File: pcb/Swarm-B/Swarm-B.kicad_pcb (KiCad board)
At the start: 2 copper layers, 71.9 x 71.9 mm, 26 parts, among them J1 RX_Break, J2 5v_3Pi, J3 GND_3Pi, J4 I2C_3Pi, SW1 Bttn, U1 74LS32, U2 TSDP34138

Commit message: added sda and scl labels to pcb
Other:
- board text added: "SCL"
- board text added: "SDA"
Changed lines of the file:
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@@
   (general
     (thickness 1.6)
-    (drawings 15)
+    (drawings 17)
     (tracks 217)
     (zones 0)
@@
   (page A4)
   (layers
-    (0 F.Cu signal)
-    (31 B.Cu signal)
+    (0 F.Cu signal hide)
+    (31 B.Cu signal hide)
     (32 B.Adhes user hide)
     (33 F.Adhes user hide)
@@
     (visible_elements 7FFFFFFF)
     (pcbplotparams
-      (layerselection 0x010fc_ffffffff)
+      (layerselection 0x01030_ffffffff)
       (usegerberextensions false)
       (usegerberattributes false)
@@
       (outputformat 1)
       (mirror false)
-      (drillshape 1)
+      (drillshape 0)
       (scaleselection 1)
-      (outputdirectory ""))
+      (outputdirectory "Gerbers/"))
   )
   (net 0 "")
@@
     )
   )
+  (gr_text SDA (at 127 105.664 90) (layer B.SilkS)
+    (effects (font (size 1.5 1.5) (thickness 0.3)) (justify mirror))
+  )
+  (gr_text SCL (at 129.794 105.664 90) (layer B.SilkS)
+    (effects (font (size 1.5 1.5) (thickness 0.3)) (justify mirror))
+  )
   (gr_text BLK (at 123.19 86.614) (layer B.SilkS)
     (effects (font (size 1.5 1.5) (thickness 0.3)) (justify mirror))
@@
   (segment (start 133.48863 75.438) (end 132.08 75.438) (width 0.25) (layer F.Cu) (net 0))
   (segment (start 134.62 75.438) (end 133.48863 75.438) (width 0.25) (layer F.Cu) (net 0))
-  (via (at 135.636 126.492) (size 0.8) (drill 0.4) (layers F.Cu B.Cu) (net 33))
-  (via (at 129.286 94.234) (size 0.8) (drill 0.4) (layers F.Cu B.Cu) (net 33))
-  (via (at 114.554 99.568) (size 0.8) (drill 0.4) (layers F.Cu B.Cu) (net 33))
-  (via (at 119.634 71.374) (size 0.8) (drill 0.4) (layers F.Cu B.Cu) (net 33))
   (segment (start 123.760001 120.333999) (end 124.46 119.634) (width 0.25) (layer F.Cu) (net 4))
   (segment (start 123.434999 120.659001) (end 123.760001 120.333999) (width 0.25) (layer F.Cu) (net 4))
@@
   (segment (start 124.46 113.564051) (end 120.447011 109.551062) (width 0.25) (layer B.Cu) (net 32))
   (segment (start 124.46 114.554) (end 124.46 113.564051) (width 0.25) (layer B.Cu) (net 32))
+  (via (at 135.636 126.492) (size 0.8) (drill 0.4) (layers F.Cu B.Cu) (net 33))
+  (via (at 129.286 94.234) (size 0.8) (drill 0.4) (layers F.Cu B.Cu) (net 33))
+  (via (at 114.554 99.568) (size 0.8) (drill 0.4) (layers F.Cu B.Cu) (net 33))
+  (via (at 119.634 71.374) (size 0.8) (drill 0.4) (layers F.Cu B.Cu) (net 33))
   (segment (start 129.54 86.614) (end 127 86.614) (width 0.25) (layer F.Cu) (net 33))
   (segment (start 145.571001 86.389001) (end 144.526 85.344) (width 0.25) (layer F.Cu) (net 33))

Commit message: update to readme
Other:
- board text added: "github.com/paulodowd/Swarm-Bs"
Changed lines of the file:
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@@
   (general
     (thickness 1.6)
-    (drawings 17)
+    (drawings 18)
     (tracks 217)
     (zones 0)
@@
     (36 B.SilkS user)
     (37 F.SilkS user)
-    (38 B.Mask user hide)
-    (39 F.Mask user hide)
+    (38 B.Mask user)
+    (39 F.Mask user)
     (40 Dwgs.User user hide)
     (41 Cmts.User user hide)
@@
     (visible_elements 7FFFFFFF)
     (pcbplotparams
-      (layerselection 0x01030_ffffffff)
+      (layerselection 0x010f0_ffffffff)
       (usegerberextensions false)
       (usegerberattributes false)
@@
     (descr "LED, diameter 3.0mm z-position of LED center 2.0mm, 2 pins")
     (tags "LED diameter 3.0mm z-position of LED center 2.0mm 2 pins")
-    (fp_text reference D1 (at 1.27 -1.96 18) (layer F.SilkS)
-      (effects (font (size 1 1) (thickness 0.15)))
-    )
-    (fp_text value IR_LED (at 0.941884 -2.89882 18) (layer F.Fab)
+    (fp_text reference D1 (at -1.521803 0.573822 18) (layer F.SilkS)
+      (effects (font (size 1 1) (thickness 0.15)))
+    )
+    (fp_text value IR_LED (at 5.706955 0.518945 18) (layer F.Fab)
       (effects (font (size 1 1) (thickness 0.15)))
     )
@@
     (descr "Resistor, Axial_DIN0204 series, Axial, Horizontal, pin pitch=5.08mm, 0.167W, length*diameter=3.6*1.6mm^2, http://cdn-reichelt.de/documents/datenblatt/B400/1_4W%23YAG.pdf")
     (tags "Resistor Axial_DIN0204 series Axial Horizontal pin pitch 5.08mm 0.167W length 3.6mm diameter 1.6mm")
-    (fp_text reference R2 (at 2.54 -1.92 90) (layer F.SilkS)
+    (fp_text reference R2 (at -1.524 0 90) (layer F.SilkS)
       (effects (font (size 1 1) (thickness 0.15)))
     )
@@
     (descr "Resistor, Axial_DIN0204 series, Axial, Horizontal, pin pitch=5.08mm, 0.167W, length*diameter=3.6*1.6mm^2, http://cdn-reichelt.de/documents/datenblatt/B400/1_4W%23YAG.pdf")
     (tags "Resistor Axial_DIN0204 series Axial Horizontal pin pitch 5.08mm 0.167W length 3.6mm diameter 1.6mm")
-    (fp_text reference R3 (at 2.54 -1.92 90) (layer F.SilkS)
+    (fp_text reference R3 (at -1.524 0 90) (layer F.SilkS)
       (effects (font (size 1 1) (thickness 0.15)))
     )
@@
     (descr "Resistor, Axial_DIN0204 series, Axial, Horizontal, pin pitch=5.08mm, 0.167W, length*diameter=3.6*1.6mm^2, http://cdn-reichelt.de/documents/datenblatt/B400/1_4W%23YAG.pdf")
     (tags "Resistor Axial_DIN0204 series Axial Horizontal pin pitch 5.08mm 0.167W length 3.6mm diameter 1.6mm")
-    (fp_text reference R4 (at 2.54 -1.92 90) (layer F.SilkS)
+    (fp_text reference R4 (at -1.524 0 90) (layer F.SilkS)
       (effects (font (size 1 1) (thickness 0.15)))
     )
@@
     )
   )
+  (gr_text github.com/paulodowd/Swarm-Bs (at 118.872 124.46) (layer F.SilkS)
+    (effects (font (size 1 1) (thickness 0.15)))
+  )
   (gr_text SDA (at 127 105.664 90) (layer B.SilkS)

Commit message: update
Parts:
- R1, R2, R3, R4, R6: footprint Resistor_THT:R_Axial_DIN0204_L3.6mm_D1.6mm_P5.08mm_Horizontal -> Resistor_THT:R_Axial_DIN0204_L3.6mm_D1.6mm_P7.62mm_Horizontal
- U1: footprint Package_DIP:DIP-16_W7.62mm_Socket -> Package_DIP:DIP-14_W7.62mm_Socket
- moved J1 5.00 mm to (127.8, 94.5), turned to 0 degrees
- moved R2 2.79 mm to (124.5, 111.8)
- moved R3 2.79 mm to (116.8, 111.8)
- moved R4 2.79 mm to (120.7, 111.8)
- moved J2 2.54 mm to (132.1, 89.2)
- moved J3 2.54 mm to (132.1, 86.6)
- moved J4 2.54 mm to (129.5, 101.9)
- moved D7 2.03 mm to (135.6, 89.2)
- moved R1 1.93 mm to (93.5, 97.3)
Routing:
- net GND: track 54.0 -> 65.5 mm
- net Net-(A1-Pad2): track 51.4 -> 41.7 mm
- net Net-(J1-Pad1): track 11.6 -> 5.58 mm
- net Net-(A1-Pad1): track 48.9 -> 54.4 mm
- net Net-(A1-Pad7): track 56.8 -> 62.2 mm
- net +5V: track 100.2 -> 96.6 mm
- net Net-(D6-Pad1): track 29.6 -> 26.8 mm
- net Net-(D6-Pad3): track 29.1 -> 26.4 mm
- net Net-(A1-Pad24): track 22.2 -> 24.7 mm
- net Net-(A1-Pad23): track 18.3 -> 20.9 mm
- net (no net): track 2.54 -> 0.00 mm
- net Net-(D6-Pad4): track 28.0 -> 25.6 mm
- net Net-(A1-Pad26): track 26.5 -> 24.4 mm
- net Net-(R1-Pad2): track 7.11 -> 8.19 mm
- net Net-(D1-Pad1): track 217.7 -> 218.7 mm
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
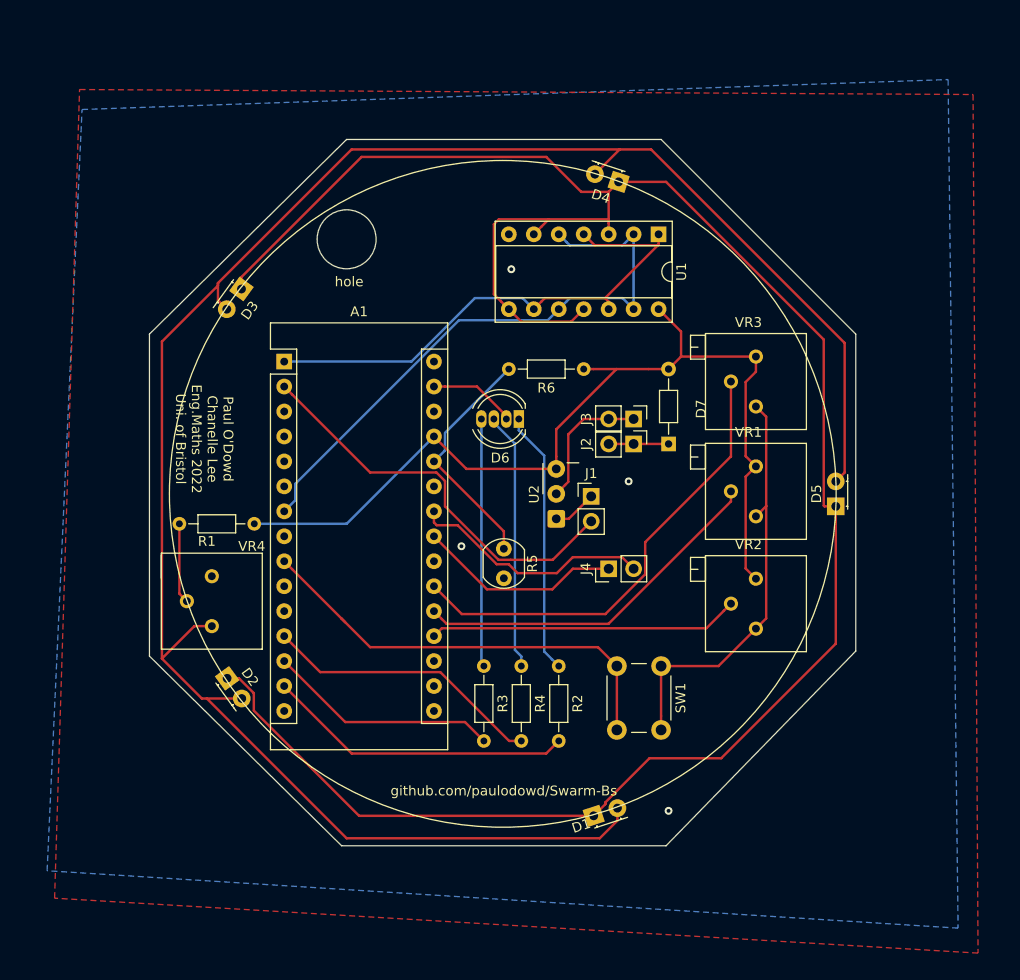
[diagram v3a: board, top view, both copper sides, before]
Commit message: altered pcb to house ICs on the underside
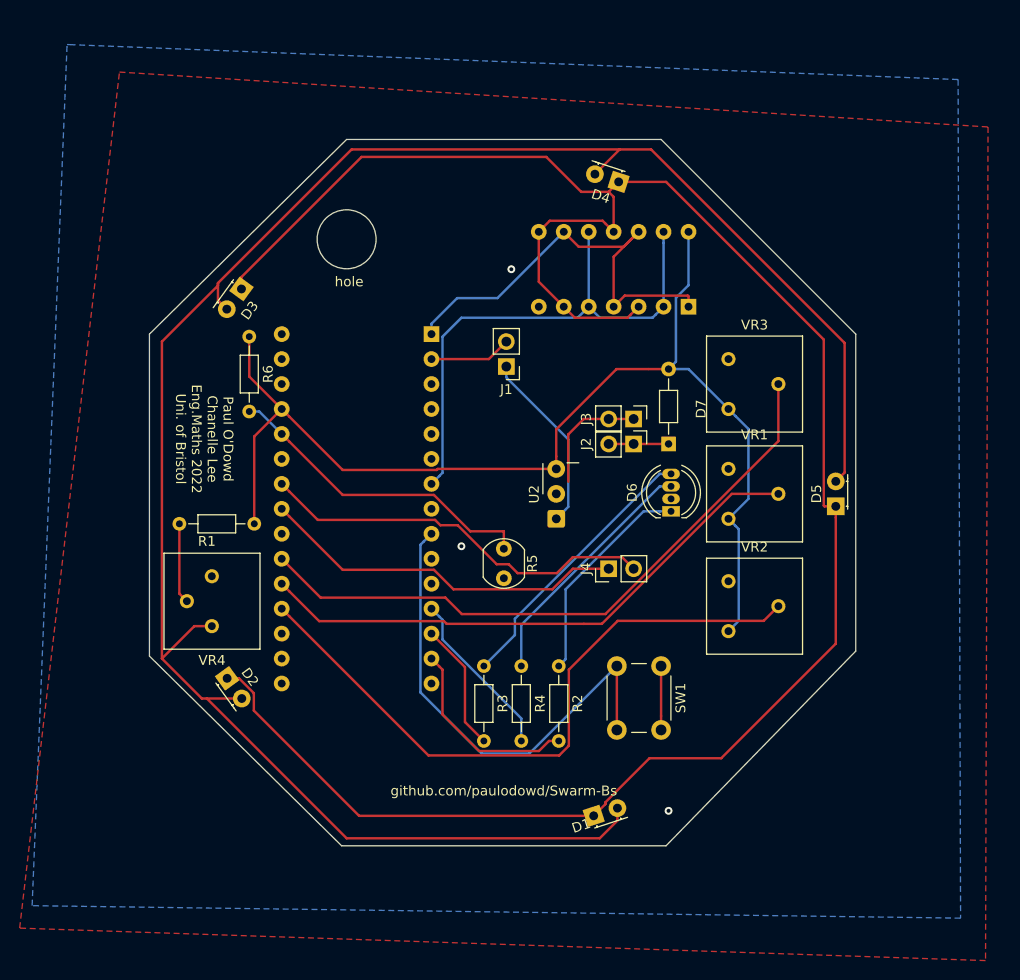
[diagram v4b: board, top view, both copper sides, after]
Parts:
- A1, U1: moved to B.Cu
- VR1, VR2, VR3: footprint Potentiometer_THT:Potentiometer_Bourns_3299P_Horizontal -> Potentiometer_THT:Potentiometer_Bourns_3386F_Vertical
- VR4: footprint Potentiometer_THT:Potentiometer_Bourns_3299P_Horizontal -> Potentiometer_THT:Potentiometer_Bourns_3386P_Vertical
- moved R6 34.2 mm to (93.0, 78.2), turned to 270 degrees
- moved D6 18.1 mm to (135.9, 96.0), turned to 90 degrees
- moved J1 15.8 mm to (119.1, 81.3), turned to 180 degrees
- moved A1 15.2 mm to (111.5, 78.0), turned to 180 degrees
- moved U1 7.97 mm to (137.7, 75.2), turned to 90 degrees
- moved VR1 6.02 mm to (141.7, 96.8)
- moved VR3 6.02 mm to (141.7, 85.6)
- moved VR2 6.02 mm to (141.7, 108.2)
- turned VR4 to 180 degrees
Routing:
- net GND: track 65.5 -> 18.6 mm, vias 4 -> 3
- net Net-(A1-Pad19): track 31.6 -> 67.6 mm
- net Net-(A1-Pad2): track 41.7 -> 8.36 mm
- net +5V: track 96.6 -> 117.9 mm
- net Net-(A1-Pad20): track 36.9 -> 57.7 mm
- net Net-(A1-Pad21): track 47.6 -> 66.0 mm
- net Net-(A1-Pad23): track 20.9 -> 37.5 mm
- net Net-(A1-Pad24): track 24.7 -> 40.7 mm
- net Net-(J1-Pad1): track 5.58 -> 19.7 mm
- net Net-(A1-Pad14): track 31.3 -> 19.9 mm
- net Net-(A1-Pad12): track 28.5 -> 17.2 mm
- net Net-(A1-Pad13): track 23.7 -> 13.1 mm
- net Net-(A1-Pad1): track 54.4 -> 45.1 mm
- net Net-(A1-Pad26): track 24.4 -> 32.7 mm
- net Net-(A1-Pad7): track 62.2 -> 55.4 mm
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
